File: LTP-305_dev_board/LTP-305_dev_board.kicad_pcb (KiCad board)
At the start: 2 copper layers, 28 parts, among them J1 Conn_01x14, J10 Conn_01x04, J11 Conn_01x04, J12 Conn_01x04, J13 Conn_01x04, J14 Conn_01x04, J15 Conn_01x04, J2 Conn_01x14, J3 Conn_01x14, J4 Conn_01x14, J5 Conn_01x07, J6 Conn_01x07, J7 Conn_01x04, J8 Conn_01x04, J9 Conn_01x04, U1 IS31FL3731-SA

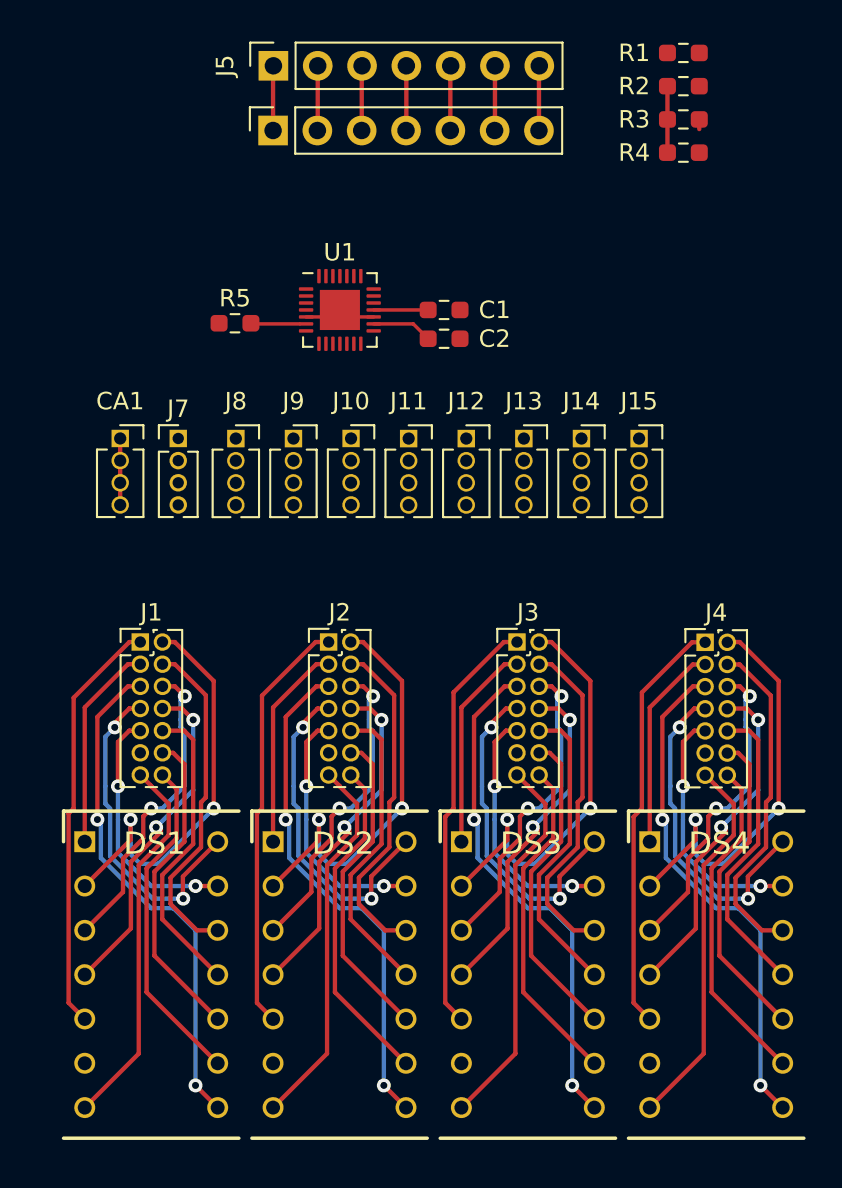
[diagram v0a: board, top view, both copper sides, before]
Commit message: Changes in schematics and PCB layout
Added power control LED
Finished schematics
New PCB layout
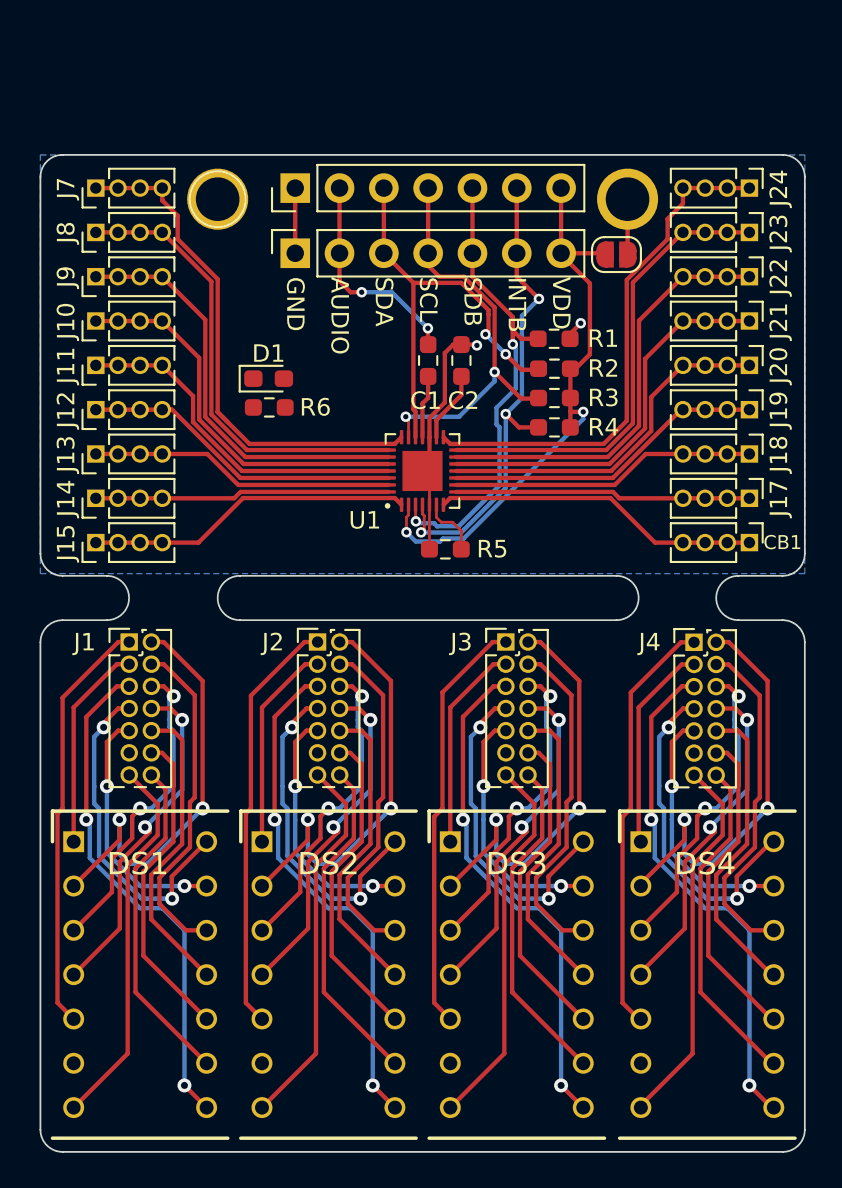
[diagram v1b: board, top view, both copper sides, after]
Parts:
- removed CA1: Conn_01x04, Connector_PinSocket_1.27mm:PinSocket_1x04_P1.27mm_Vertical
- added ?: , , F.Cu at (160.7, 47.0)
- added CB1: Conn_01x04, Connector_PinHeader_1.27mm:PinHeader_1x04_P1.27mm_Vertical, F.Cu at (167.6, 66.7)
- added D1: LED, LED_SMD:LED_0603_1608Metric_Pad1.05x0.95mm_HandSolder, F.Cu at (140.1, 57.3)
- added J17: Conn_01x04, Connector_PinHeader_1.27mm:PinHeader_1x04_P1.27mm_Vertical, F.Cu at (167.6, 64.1)
- added J18: Conn_01x04, Connector_PinHeader_1.27mm:PinHeader_1x04_P1.27mm_Vertical, F.Cu at (167.6, 61.6)
- added J19: Conn_01x04, Connector_PinHeader_1.27mm:PinHeader_1x04_P1.27mm_Vertical, F.Cu at (167.6, 59.1)
- added J20: Conn_01x04, Connector_PinHeader_1.27mm:PinHeader_1x04_P1.27mm_Vertical, F.Cu at (167.6, 56.5)
- added J21: Conn_01x04, Connector_PinHeader_1.27mm:PinHeader_1x04_P1.27mm_Vertical, F.Cu at (167.6, 54.0)
- added J22: Conn_01x04, Connector_PinHeader_1.27mm:PinHeader_1x04_P1.27mm_Vertical, F.Cu at (167.6, 51.4)
- added J23: Conn_01x04, Connector_PinHeader_1.27mm:PinHeader_1x04_P1.27mm_Vertical, F.Cu at (167.6, 48.9)
- added J24: Conn_01x04, Connector_PinHeader_1.27mm:PinHeader_1x04_P1.27mm_Vertical, F.Cu at (167.6, 46.4)
- added R6: R, Resistor_SMD:R_0603_1608Metric_Pad0.98x0.95mm_HandSolder, F.Cu at (140.1, 58.9)
- added REF**: Pin_D1.3mm_L11.0mm, Connector_Pin:Pin_D1.3mm_L11.0mm, F.Cu at (137.2, 47.0)
- added REF**: SolderJumper-2_P1.3mm_Open_RoundedPad1.0x1.5mm, Jumper:SolderJumper-2_P1.3mm_Open_RoundedPad1.0x1.5mm, F.Cu at (160.0, 50.2)
- DS1, DS2, DS3, DS4: footprint LTP-305:DIPS762W50P254L1850H400Q14N -> LTP305:DIPS762W50P254L1850H400Q14N
- J10, J11, J12, J13, J14, J15, J8, J9: footprint Connector_PinSocket_1.27mm:PinSocket_1x04_P1.27mm_Vertical -> Connector_PinHeader_1.27mm:PinHeader_1x04_P1.27mm_Vertical
- J5: footprint Connector_PinSocket_2.54mm:PinSocket_1x07_P2.54mm_Vertical -> Connector_PinHeader_2.54mm:PinHeader_1x07_P2.54mm_Vertical
- moved J15 31.7 mm to (130.2, 66.7), turned to 90 degrees
- moved J14 28.0 mm to (130.2, 64.1), turned to 90 degrees
- moved J13 24.6 mm to (130.2, 61.6), turned to 90 degrees
- moved J12 21.3 mm to (130.2, 59.1), turned to 90 degrees
- moved J11 18.4 mm to (130.2, 56.5), turned to 90 degrees
- moved R1 18.0 mm to (156.4, 55.0), turned to 0 degrees
- moved R2 17.8 mm to (156.5, 56.7), turned to 180 degrees
- moved R5 17.7 mm to (150.2, 67.1)
- moved R3 17.6 mm to (156.5, 58.4), turned to 180 degrees
- moved R4 17.4 mm to (156.5, 60.1), turned to 180 degrees
- moved J10 16.1 mm to (130.2, 54.0), turned to 90 degrees
- moved J7 15.1 mm to (130.2, 46.4), turned to 90 degrees
- moved J9 14.6 mm to (130.2, 51.4), turned to 90 degrees
- moved J8 14.3 mm to (130.2, 48.9), turned to 90 degrees
- moved U1 10.4 mm to (148.9, 62.6), turned to 90 degrees
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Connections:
- J11 pad 1: Net-(J11-Pad1) -> CA5
- J11 pad 2: Net-(J11-Pad1) -> CA5
- J11 pad 3: Net-(J11-Pad1) -> CA5
- J11 pad 4: Net-(J11-Pad1) -> CA5
- J12 pad 1: Net-(J12-Pad1) -> CA6
- J12 pad 2: Net-(J12-Pad1) -> CA6
- J12 pad 3: Net-(J12-Pad1) -> CA6
- J12 pad 4: Net-(J12-Pad1) -> CA6
- J13 pad 1: Net-(J13-Pad1) -> CA7
- J13 pad 2: Net-(J13-Pad1) -> CA7
- J13 pad 3: Net-(J13-Pad1) -> CA7
- J13 pad 4: Net-(J13-Pad1) -> CA7
- J14 pad 1: Net-(J14-Pad1) -> CA8
- J14 pad 2: Net-(J14-Pad1) -> CA8
- J14 pad 3: Net-(J14-Pad1) -> CA8
- J14 pad 4: Net-(J14-Pad1) -> CA8
- J15 pad 1: Net-(J15-Pad1) -> CA9
- J15 pad 2: Net-(J15-Pad1) -> CA9
- J15 pad 3: Net-(J15-Pad1) -> CA9
- J15 pad 4: Net-(J15-Pad1) -> CA9
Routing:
- net CB9: track 0.00 -> 29.7 mm
- net VDD: track 7.53 -> 36.9 mm, vias 0 -> 2
- net CB8: track 0.00 -> 26.7 mm
- net CA2: track 0.00 -> 26.4 mm
- net CA1: track 3.81 -> 30.2 mm
- net CB7: track 0.00 -> 24.6 mm
- net INTB: track 3.72 -> 28.3 mm, vias 0 -> 3
- net CA3: track 0.00 -> 24.3 mm
- net SDB: track 3.72 -> 27.1 mm, vias 0 -> 2
- net CB6: track 0.00 -> 22.5 mm
- net CA4: track 0.00 -> 22.2 mm
- net SDA: track 3.72 -> 25.4 mm, vias 0 -> 2
- net CB5: track 0.00 -> 20.4 mm
- net CA5: track 0.00 -> 20.2 mm
- net SCL: track 4.27 -> 23.8 mm, vias 0 -> 2
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- added copper zone on B.Cu, net GND
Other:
- board outline added: 43.8 x 57.1 mm
- board text added: "AUDIO"
- board text added: "GND"
- board text added: "INTB"
- board text added: "SCL"
- board text added: "SDA"
- board text added: "SDB"
- board text added: "VDD"

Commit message: Board layout update
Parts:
- removed the REF** at (137.2, 47.0)
- added ?: , , F.Cu at (137.2, 47.0)
- moved J6 0.52 mm to (159.9, 49.5)
- moved D1 0.48 mm to (139.6, 57.3)
- moved R6 0.48 mm to (139.6, 58.9), turned to 180 degrees
- renumbered J7 to CA1, J8 to CA2, J9 to CA3, J10 to CA4, J11 to CA5, J12 to CA6, J13 to CA7, J14 to CA8, J15 to CA9, J17 to CB2, J18 to CB3, J19 to CB4, J20 to CB5, J21 to CB6, J22 to CB7, J23 to CB8, J24 to CB9
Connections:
- D1 pad 1: unconnected-(D1-Pad1) -> Net-(D1-Pad1)
- D1 pad 2: unconnected-(D1-Pad2) -> GND
- R6 pad 1: unconnected-(R6-Pad1) -> VDD
- R6 pad 2: unconnected-(R6-Pad2) -> Net-(D1-Pad1)
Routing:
- net VDD: track 36.9 -> 47.8 mm, vias 2 -> 3
- net Net-(D1-Pad1): track 0.00 -> 1.72 mm
- net GND: track 19.2 -> 19.8 mm, vias 2 -> 7
- net SDB: track 27.1 -> 26.6 mm
- net SCL: track 23.8 -> 23.3 mm
- net INTB: track 28.3 -> 27.8 mm
- net SDA: track 25.4 -> 24.8 mm
- net AUDIO: track 12.5 -> 12.0 mm
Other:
- board text added: "Power"

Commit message: rev 0.1 done
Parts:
- turned D1 to 180 degrees
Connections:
- D1 pad 1: Net-(D1-Pad1) -> GND
- D1 pad 2: GND -> Net-(R6-Pad2)
- R6 pad 2: Net-(D1-Pad1) -> Net-(R6-Pad2)
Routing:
- net Net-(R6-Pad2): track 0.00 -> 1.76 mm
- net Net-(D1-Pad1): track 1.72 -> 0.00 mm
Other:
- outline, holes or cut-outs redrawn
- board text added: "AC1"
- board text added: "AC2"
- board text added: "AC3"
- board text added: "AC4"
- board text added: "AC5"
- board text added: "ADP"
- board text added: "CR1"
- board text added: "CR2"
- board text added: "CR3"
- board text added: "CR4"
- board text added: "CR5"
- board text added: "CR6"
- board text added: "CR7"
- board text added: "Development board"
- board text added: "LTP-305 LED matrix"
- board text added: "rev. 01"
